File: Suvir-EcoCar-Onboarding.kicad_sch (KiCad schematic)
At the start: 54 parts, among them J1 Conn_01x04_Pin, J2 USB_B_Micro, J3 Conn_01x04_Pin, J4 Conn_01x04_Pin, J5 Conn_01x04_Pin, SW1 SW_SPDT, U1 STM32F103C8Tx, U2 AMS1117-3.3, U6 NHD-C0220BIZ, Y1 16MHz

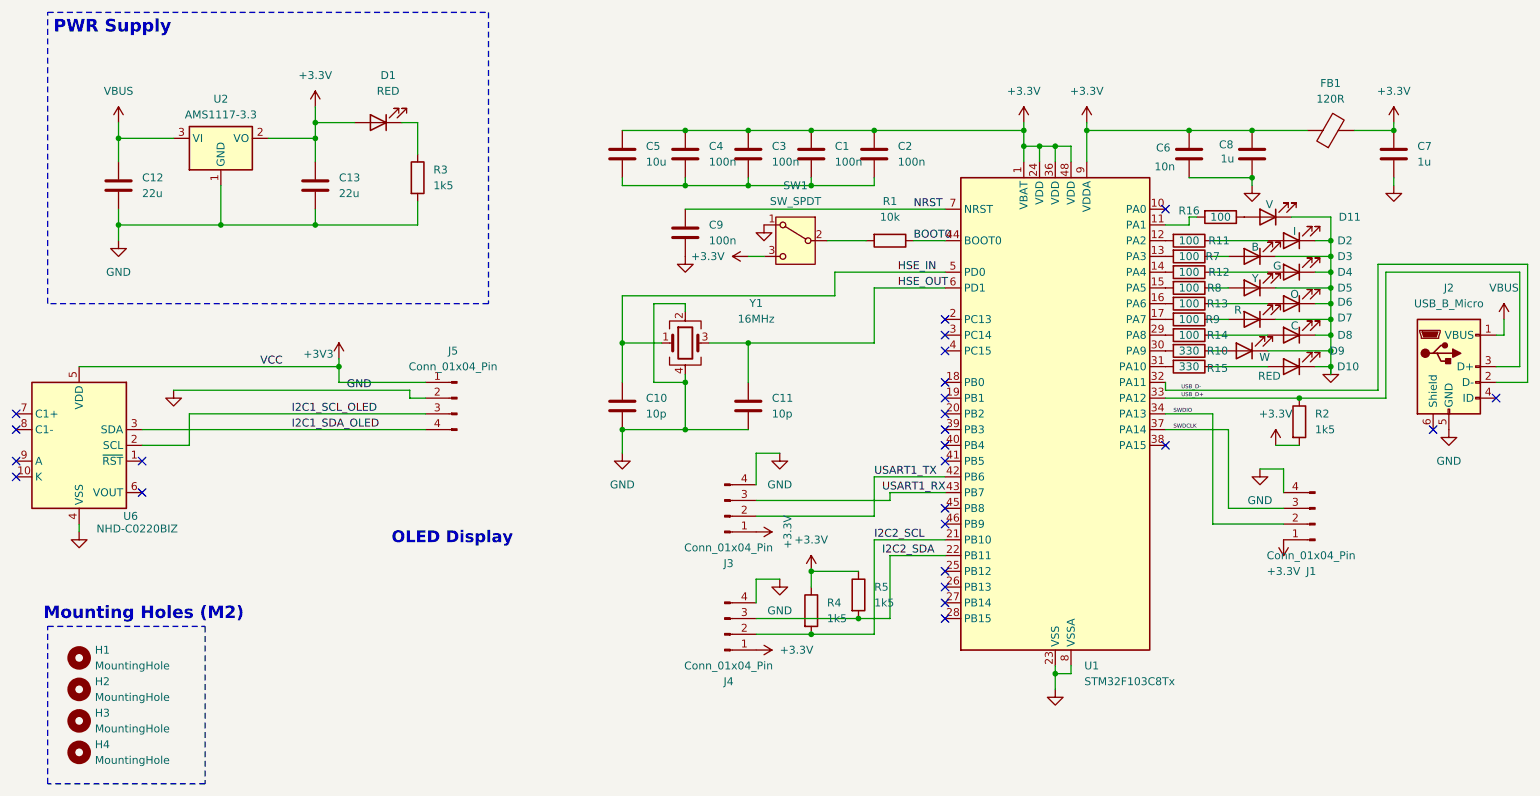
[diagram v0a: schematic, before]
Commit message: made changes wrt routing
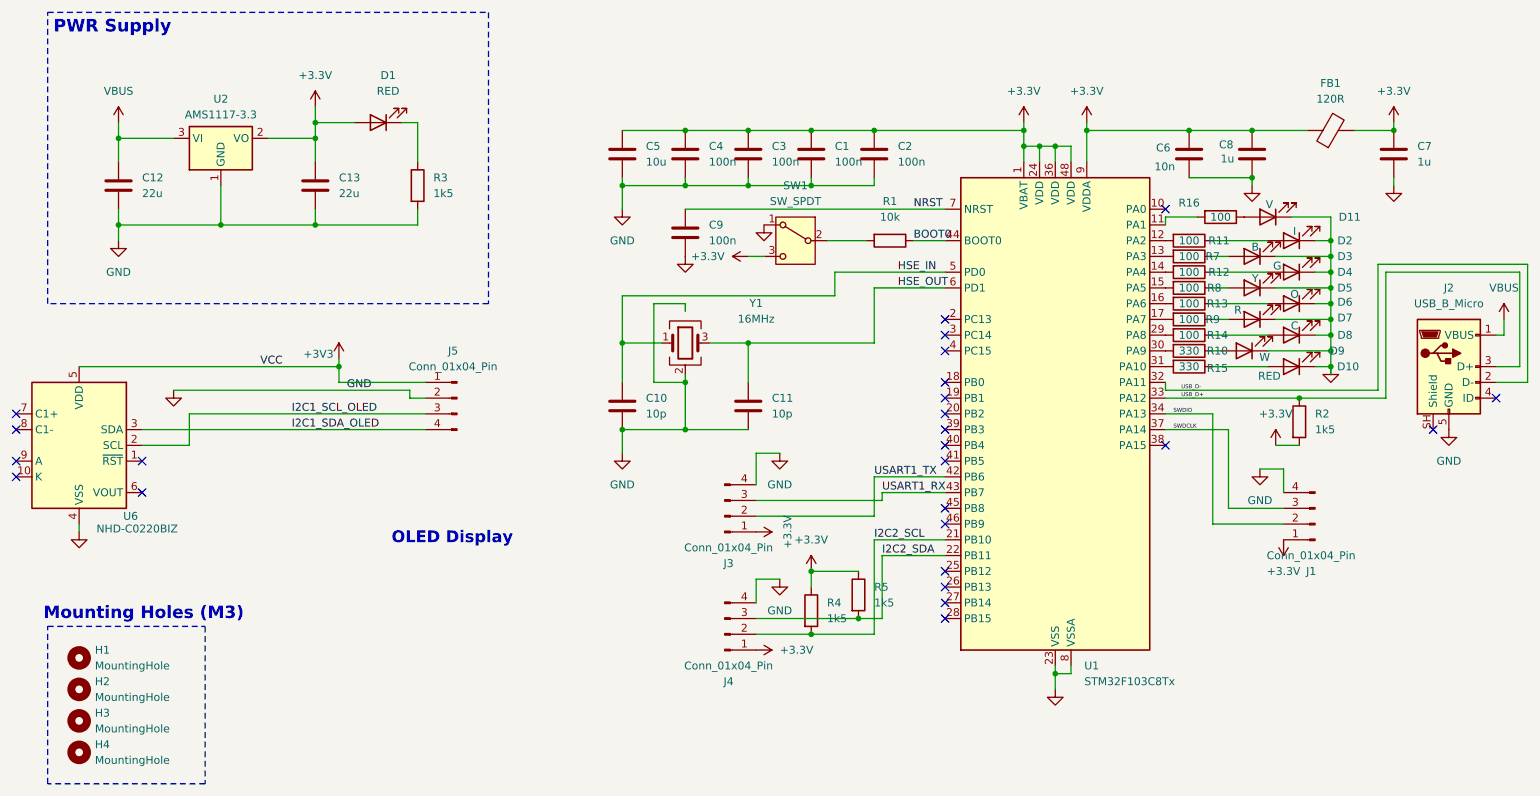
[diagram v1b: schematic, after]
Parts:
- H1, H2, H3, H4: footprint MountingHole:MountingHole_2.2mm_M2 -> MountingHole:MountingHole_3.2mm_M3
- U6: footprint Display:Adafruit_SSD1306_No_Mounting_Holes -> Display:NHD-C0220BiZ
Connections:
- net GND: now also C1.2, C2.2, C3.2, C4.2, C5.2
- net I2C2_SDA: now also J4.3 (Pin_3), R5.2, U1.22 (PB11)
- net USART1_RX: now also J3.3 (Pin_3), U1.43 (PB7)
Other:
- note added: "Mounting Holes (M3)"
- note removed: "Mounting Holes (M2)"
- moved on the sheet: R3
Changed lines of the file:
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@@
 		(date "24-03-26")
 	)
-	(text "Mounting Holes (M2)\n"
+	(text "Mounting Holes (M3)\n"
 		(exclude_from_sim no)
 		(at 39.624 126.238 0)
@@
 	)
 	(junction
-		(at 154.94 127)
-		(diameter 0)
-		(color 0 0 0 0)
-	)
-	(junction
 		(at 147.32 129.54)
 		(diameter 0)
@@
 	)
 	(junction
+		(at 116.84 57.15)
+		(diameter 0)
+		(color 0 0 0 0)
+	)
+	(junction
 		(at 127 96.52)
 		(diameter 0)
@@
 	)
 	(junction
+		(at 154.94 127)
+		(diameter 0)
+		(color 0 0 0 0)
+	)
+	(junction
 		(at 218.44 55.88)
 		(diameter 0)
@@
 	(wire
 		(pts
-			(xy 204.47 63.5) (xy 208.28 63.5)
+			(xy 204.47 62.23) (xy 209.55 62.23)
 		)
 		(stroke
@@
 	(wire
 		(pts
-			(xy 160.02 127) (xy 160.02 116.84)
+			(xy 158.75 127) (xy 158.75 116.84)
 		)
 		(stroke
@@
 	(wire
 		(pts
+			(xy 116.84 57.15) (xy 116.84 60.96)
+		)
+		(stroke
+			(width 0)
+			(type default)
+		)
+	)
+	(wire
+		(pts
 			(xy 208.28 55.88) (xy 218.44 55.88)
 		)
@@
 	(wire
 		(pts
-			(xy 160.02 107.95) (xy 160.02 106.68)
+			(xy 158.75 107.95) (xy 158.75 106.68)
 		)
 		(stroke
@@
 	(wire
 		(pts
-			(xy 208.28 62.23) (xy 209.55 62.23)
-		)
-		(stroke
-			(width 0)
-			(type default)
-		)
-	)
-	(wire
-		(pts
 			(xy 137.16 82.55) (xy 137.16 88.9)
 		)
@@
 	(wire
 		(pts
-			(xy 160.02 116.84) (xy 168.91 116.84)
+			(xy 158.75 116.84) (xy 168.91 116.84)
 		)
 		(stroke
@@
 	(wire
 		(pts
+			(xy 204.47 62.23) (xy 204.47 63.5)
+		)
+		(stroke
+			(width 0)
+			(type default)
+		)
+	)
+	(wire
+		(pts
 			(xy 212.09 93.98) (xy 212.09 111.76)
 		)
@@
 	(wire
 		(pts
-			(xy 208.28 62.23) (xy 208.28 63.5)
-		)
-		(stroke
-			(width 0)
-			(type default)
-		)
-	)
-	(wire
-		(pts
 			(xy 52.07 57.15) (xy 52.07 63.5)
 		)
@@
 	(wire
 		(pts
-			(xy 154.94 127) (xy 160.02 127)
+			(xy 154.94 127) (xy 158.75 127)
 		)
 		(stroke
@@
 	(wire
 		(pts
-			(xy 83.82 46.99) (xy 83.82 52.07)
+			(xy 83.82 46.99) (xy 83.82 53.34)
 		)
 		(stroke
@@
 	(wire
 		(pts
-			(xy 138.43 107.95) (xy 160.02 107.95)
+			(xy 138.43 107.95) (xy 158.75 107.95)
 		)
 		(stroke
@@
 	(wire
 		(pts
-			(xy 160.02 106.68) (xy 168.91 106.68)
+			(xy 158.75 106.68) (xy 168.91 106.68)
 		)
 		(stroke
@@
 	(wire
 		(pts
-			(xy 83.82 59.69) (xy 83.82 63.5)
+			(xy 83.82 60.96) (xy 83.82 63.5)
 		)
 		(stroke
@@
 			)
 		)
-		(property "Footprint" "MountingHole:MountingHole_2.2mm_M2"
+		(property "Footprint" "MountingHole:MountingHole_3.2mm_M3"
 			(at 29.21 138.43 0)
 			(hide yes)
@@
 			)
 		)
-		(property "Footprint" "MountingHole:MountingHole_2.2mm_M2"
+		(property "Footprint" "MountingHole:MountingHole_3.2mm_M3"
 			(at 29.21 143.51 0)
 			(hide yes)
@@
 	(symbol
 		(lib_id "Device:R")
-		(at 83.82 55.88 0)
+		(at 83.82 57.15 0)
 		(unit 1)
 		(body_style 1)
@@
 		(fields_autoplaced yes)
 		(property "Reference" "R3"
-			(at 86.36 54.6099 0)
+			(at 86.36 55.8799 0)
 			(show_name no)
 			(do_not_autoplace no)
@@
 		)
 		(property "Value" "1k5"
-			(at 86.36 57.1499 0)
+			(at 86.36 58.4199 0)
 			(show_name no)
 			(do_not_autoplace no)
@@
 		)
 		(property "Footprint" "Resistor_SMD:R_0402_1005Metric"
-			(at 82.042 55.88 90)
+			(at 82.042 57.15 90)
 			(hide yes)
 			(show_name no)
@@
 		)
 		(property "Datasheet" ""
-			(at 83.82 55.88 0)
+			(at 83.82 57.15 0)
 			(hide yes)
 			(show_name no)
@@
 		)
 		(property "Description" "Resistor"
-			(at 83.82 55.88 0)
+			(at 83.82 57.15 0)
 			(hide yes)
 			(show_name no)
@@
 			)
 		)
-		(property "Footprint" "MountingHole:MountingHole_2.2mm_M2"
+		(property "Footprint" "MountingHole:MountingHole_3.2mm_M3"
 			(at 29.21 133.35 0)
 			(hide yes)
@@
 			)
 		)
-		(property "Footprint" "MountingHole:MountingHole_2.2mm_M2"
+		(property "Footprint" "MountingHole:MountingHole_3.2mm_M3"
 			(at 29.21 148.59 0)
 			(hide yes)
@@
 		(pin "5"
 		)
-		(pin "6"
+		(pin "SH"
 		)
 		(pin "1"
@@
 		(dnp no)
 		(property "Reference" "R16"
-			(at 208.28 61.214 90)
+			(at 208.28 59.944 90)
 			(show_name no)
 			(do_not_autoplace no)
@@
 			)
 		)
-		(property "Footprint" "Display:Adafruit_SSD1306_No_Mounting_Holes"
+		(property "Footprint" "Display:NHD-C0220BiZ"
 			(at 29.21 114.3 0)
 			(hide yes)
@@
 					(unit 1)
 				)
+			)
+		)
+	)
+	(symbol
+		(lib_id "power:GND")
+		(at 116.84 60.96 0)
+		(unit 1)
+		(body_style 1)
+		(exclude_from_sim no)
+		(in_bom yes)
+		(on_board yes)
+		(in_pos_files yes)
+		(dnp no)
+		(fields_autoplaced yes)
+		(property "Reference" "#PWR025"
+			(at 116.84 67.31 0)
+			(hide yes)
+			(show_name no)
+			(do_not_autoplace no)
+			(effects
+				(font
+					(size 1.27 1.27)
+				)
+			)
+		)
+		(property "Value" "GND"
+			(at 116.84 66.04 0)
+			(show_name no)
+			(do_not_autoplace no)
+			(effects
+				(font
+					(size 1.27 1.27)
+				)
+			)
+		)
+		(property "Footprint" ""
+			(at 116.84 60.96 0)
+			(hide yes)
+			(show_name no)
+			(do_not_autoplace no)
+			(effects
+				(font
+					(size 1.27 1.27)
+				)
+			)
+		)
+		(property "Datasheet" ""
+			(at 116.84 60.96 0)
+			(hide yes)
+			(show_name no)
+			(do_not_autoplace no)
+			(effects
+				(font
+					(size 1.27 1.27)
+				)
+			)
+		)
+		(property "Description" "Power symbol creates a global label with name \"GND\" , ground"
+			(at 116.84 60.96 0)
+			(hide yes)
+			(show_name no)
+			(do_not_autoplace no)
+			(effects
+				(font
+					(size 1.27 1.27)
+				)
+			)
+		)
+		(pin "1"
+		)
+		(instances
+			(project "Suvir-EcoCar-Onboarding"
+				(path "/814de93a-890d-46c1-8ceb-5f8e394fffe3"
+					(reference "#PWR025")
+					(unit 1)
+				)
